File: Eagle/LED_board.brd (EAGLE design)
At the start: 21.1 x 33.8 mm, 38 parts, among them P1 P1, P2 P2

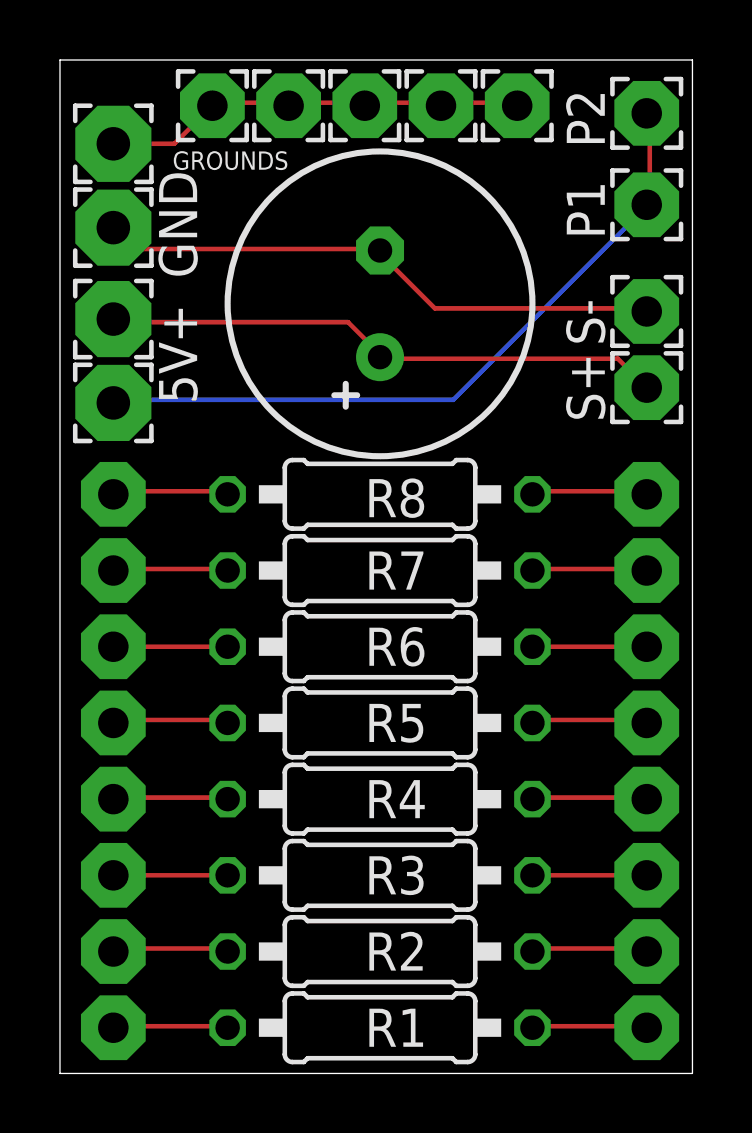
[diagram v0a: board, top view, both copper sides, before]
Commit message: Changed the board design so it is cheaper at oshpark and no longer has the unused components
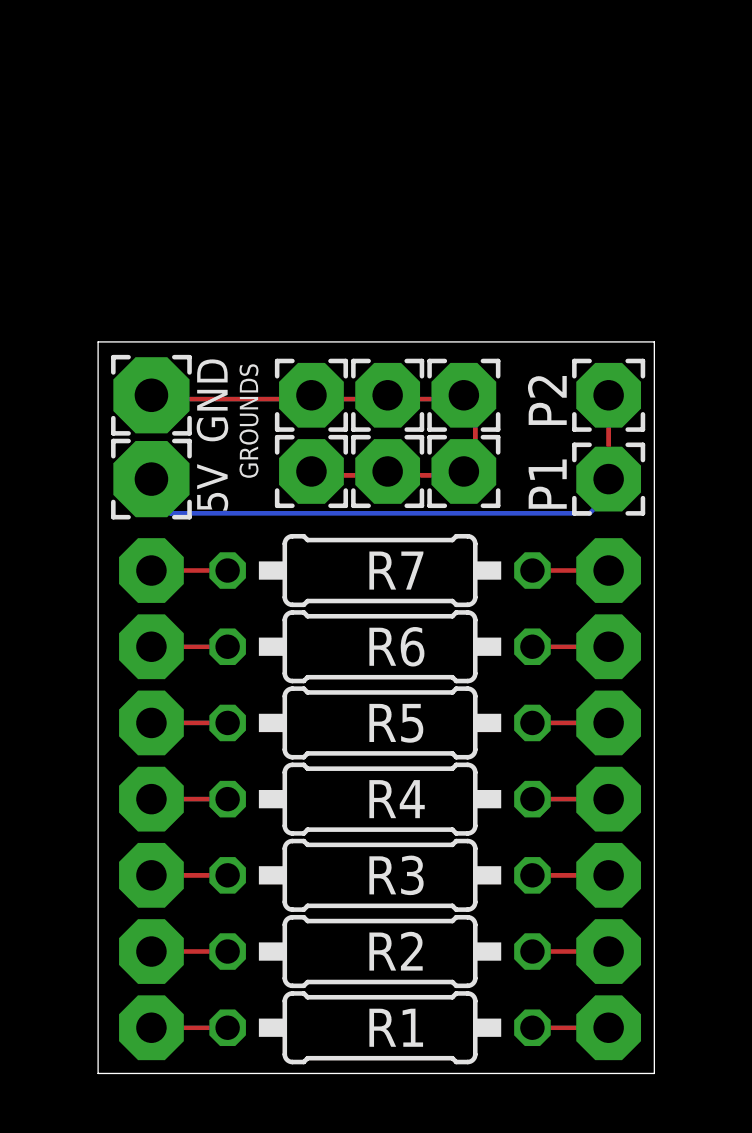
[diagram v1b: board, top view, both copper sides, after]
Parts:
- removed +: 5+, wirepad:2,54/1,1
- removed 8: 8, wirepad:2,15/1,0
- removed A8: A8, wirepad:2,15/1,0
- removed C1: 480, CAP_ELECTROLYTIC:CELEC_3.5MM_10MM
- removed GND1: GND, wirepad:2,54/1,1
- removed R8: 220, resistor:0207/10
- removed S+: S+, wirepad:2,15/1,0
- removed S-: S-, wirepad:2,15/1,0
- added G2: G5, wirepad:2,15/1,0
- moved GROUNDS 12.6 mm to (9.14, 21.1)
- moved G5 12.2 mm to (11.7, 21.1)
- moved G1 9.81 mm to (11.7, 23.6)
- moved G3 9.81 mm to (14.2, 23.6)
- moved G4 9.68 mm to (9.14, 23.6)
- moved P2 9.48 mm to (19.1, 23.6)
- moved P1 9.23 mm to (19.1, 20.8)
- moved GND 8.48 mm to (3.81, 23.6)
- moved 5V 2.84 mm to (3.81, 20.8)
- moved A1 1.27 mm to (3.81, 2.54)
- moved A2 1.27 mm to (3.81, 5.08)
- moved A3 1.27 mm to (3.81, 7.62)
- moved A4 1.27 mm to (3.81, 10.2)
- moved A5 1.27 mm to (3.81, 12.7)
- moved A6 1.27 mm to (3.81, 15.2)
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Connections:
- removed net N$17: 8.1, R8.2
- removed net N$18: A8.1, R8.1
- removed net N$19: +.1, C1.+, S+.1
- removed net N$20: C1.-, GND1.1, S-.1
- net N$4: now also G2.1
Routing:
- net N$20: track 19.1 -> 0.00 mm
- net N$19: track 18.8 -> 0.00 mm
- net N$4: track 14.4 -> 18.8 mm
- net N$1: track 23.7 -> 19.6 mm
- net N$17: track 3.91 -> 0.00 mm
- net N$18: track 3.91 -> 0.00 mm
- net N$12: track 3.91 -> 2.54 mm
- net N$11: track 3.91 -> 2.54 mm
- net N$5: track 3.91 -> 2.54 mm
- net N$6: track 3.91 -> 2.54 mm
- net N$9: track 3.84 -> 2.54 mm
- net N$10: track 3.84 -> 2.54 mm
- net N$2: track 3.84 -> 2.54 mm
- net N$3: track 3.84 -> 2.54 mm
- net N$16: track 3.84 -> 2.54 mm
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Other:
- board size 21.1 x 33.8 mm -> 18.5 x 24.4 mm
